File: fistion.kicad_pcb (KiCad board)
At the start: 2 copper layers, 226 x 66.2 mm, 85 parts, among them J1 debug-port, J10 Conn_01x06_Male, J2 USB_C_Receptacle_USB2.0, J3 Conn_01x06_Male, J4 Conn_01x06_Male, J5 Conn_01x06_Male, J6 Conn_01x06_Male, J7 Conn_01x06_Male, J8 Conn_01x06_Male, J9 Conn_01x06_Male, K1 diode-choc, K10 diode-choc, K11 diode-choc, K12 diode-choc, K13 diode-choc, K14 diode-choc, K15 diode-choc, K16 diode-choc, K2 diode-choc, K3 diode-choc, K4 diode-choc, K5 diode-choc, K6 diode-choc, K7 diode-choc, K8 diode-choc, K9 diode-choc, SW1 SW_Push, U1 MT25QL128ABA1ESE, U2 ms88sf3-nrf52840, U3 LSM6DS3, U4 XC6220B331MR, U5 TLV70237_SOT23-5, U6 SRV05-4, U8 PMW3610, U9 MCP1804x-1802xMB

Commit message: no screen
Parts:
- removed JP2: jumper, Jumper:SolderJumper-3_P1.3mm_Open_RoundedPad1.0x1.5mm
- removed JP3: ~, Jumper:SolderJumper-2_P1.3mm_Open_RoundedPad1.0x1.5mm
- removed JP4: SolderJumper_2_Open, Jumper:SolderJumper-2_P1.3mm_Open_RoundedPad1.0x1.5mm
- removed LCD1: adafruit-sharp-memory-display-no-useless, display:adafruit-sharp-memory-display-1.3in-no-mounting-no-useless
- added R7: 1M, Resistor_SMD:R_0603_1608Metric, F.Cu at (120.5, 105.7)
- added REF**: MountingHole_2.2mm_M2, MountingHole:MountingHole_2.2mm_M2, F.Cu at (108.7, 81.7)
- added REF**: MountingHole_2.2mm_M2, MountingHole:MountingHole_2.2mm_M2, F.Cu at (106.2, 115.7)
- added REF**: MountingHole_2.2mm_M2, MountingHole:MountingHole_2.2mm_M2, F.Cu at (136.7, 115.7)
- added REF**: MountingHole_2.2mm_M2, MountingHole:MountingHole_2.2mm_M2, F.Cu at (109.7, 37.7)
- added REF**: nothing, misc:nothing, F.Cu at (82.7, 54.2)
- added REF**: MountingHole_2.2mm_M2, MountingHole:MountingHole_2.2mm_M2, F.Cu at (134.2, 82.2)
- added REF**: MountingHole_2.2mm_M2, MountingHole:MountingHole_2.2mm_M2, F.Cu at (133.2, 37.7)
- added SW2: RotaryEncoder_Switch, switch:EVQWGD001, F.Cu at (121.5, 77.7)
- C4: footprint Capacitor_THT:CP_Radial_D13.0mm_P5.00mm -> Capacitor_THT:CP_Radial_D16.0mm_P7.50mm
- C8: value 47uF -> 4.7uF
- moved D2 142.4 mm to (96.6, 26.5)
- moved J10 142.4 mm to (130.6, 20.3)
- moved J3 142.4 mm to (58.6, 20.3)
- moved J4 142.4 mm to (92.6, 20.3)
- moved J6 142.4 mm to (90.6, 20.3)
- moved K13 142.4 mm to (74.6, 15.9)
- moved K16 142.4 mm to (109.7, 15.9)
- moved SC1 142.4 mm to (109.7, 20.3)
- moved J7 142.4 mm to (162.6, 20.3)
- moved J9 142.4 mm to (128.6, 20.3)
- moved K15 142.4 mm to (146.6, 15.9)
- moved JP1 24.7 mm to (122.0, 96.8), turned to 180 degrees
- moved U4 23.8 mm to (120.7, 100.5), turned to 90 degrees
- moved R21 23.7 mm to (124.2, 111.3)
- moved R22 23.7 mm to (124.2, 112.8)
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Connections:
- J5 pad 6: 3V3_nRF -> +3V3
- JP1 pad 1: 3V3_nRF -> +3V3
- R1 pad 1: 3V3_nRF -> +3V3
- U1 pad 8: 3V3_nRF -> +3V3
- U2 pad 21: DISP_~{CS} -> unconnected-(U2-Pad21)
- U2 pad 22: unconnected-(U2-Pad22) -> MOTION
- U2 pad 23: MOTION -> MOUSE_~{RST}
- U2 pad 24: MOUSE_~{RST} -> MOUSE_~{CS}
- U2 pad 25: MOUSE_~{CS} -> SCLK2
- U2 pad 26: SCLK2 -> SDIO
- U2 pad 27: SDIO -> B
- U2 pad 29: unconnected-(U2-Pad29) -> A
- U2 pad 30: unconnected-(U2-Pad30) -> ENC_PUSH
- U4 pad 3: SOLAR_OUT -> Net-(R7-Pad1)
- U7 pad 11: unconnected-(U7-Pad11) -> Net-(R7-Pad1)
- U9 pad 3: Net-(JP2-Pad2) -> SOLAR_OUT
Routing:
- net +3V3: track 0.00 -> 80.4 mm, vias 0 -> 2
- net 3V3_nRF: track 130.6 -> 78.0 mm, vias 4 -> 1
- net GND: track 11.8 -> 57.0 mm, vias 22 -> 31
- net ENC_PUSH: track 0.00 -> 40.0 mm, vias 0 -> 1
- net A: track 0.00 -> 38.7 mm, vias 0 -> 1
- net B: track 0.00 -> 37.2 mm, vias 0 -> 1
- net C2: track 168.1 -> 148.2 mm
- net +1V8: track 23.8 -> 5.05 mm
- net DISP_~{CS}: track 15.0 -> 0.00 mm, vias 1 -> 0
- net C3: track 139.3 -> 124.4 mm
- net Net-(R7-Pad1): track 0.00 -> 13.8 mm
- net SOLAR_OUT: track 57.8 -> 71.3 mm, vias 0 -> 2
- net BAT: track 85.6 -> 98.8 mm, vias 3 -> 4
- net SDIO: track 45.1 -> 34.3 mm
- net SCLK2: track 45.0 -> 35.3 mm
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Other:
- board size 226 x 66.2 mm -> 104 x 106.5 mm
- board text added: "- screen may go on top/left side"
- board text removed: "- solar & LED goes on top (top thumb?) - screen may go on top/left side"

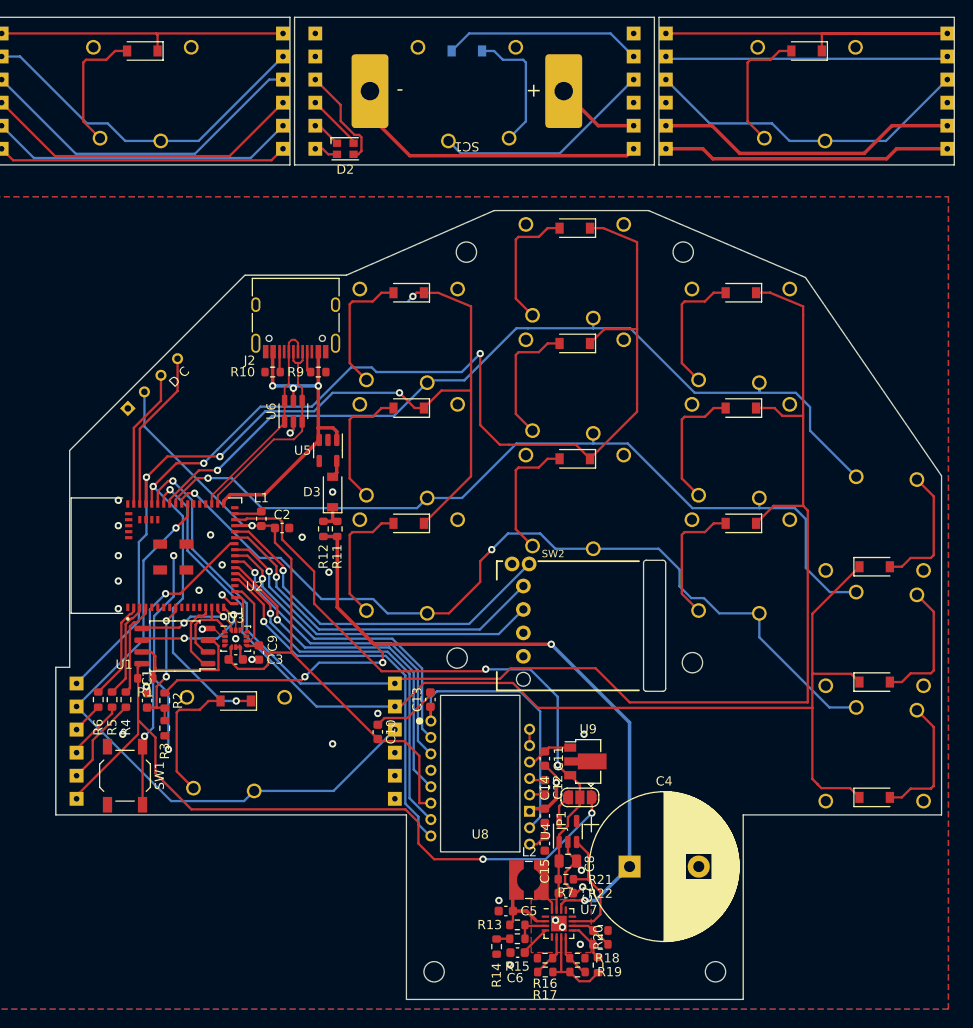
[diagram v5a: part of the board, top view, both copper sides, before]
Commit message: scroll wheel + constant current charger
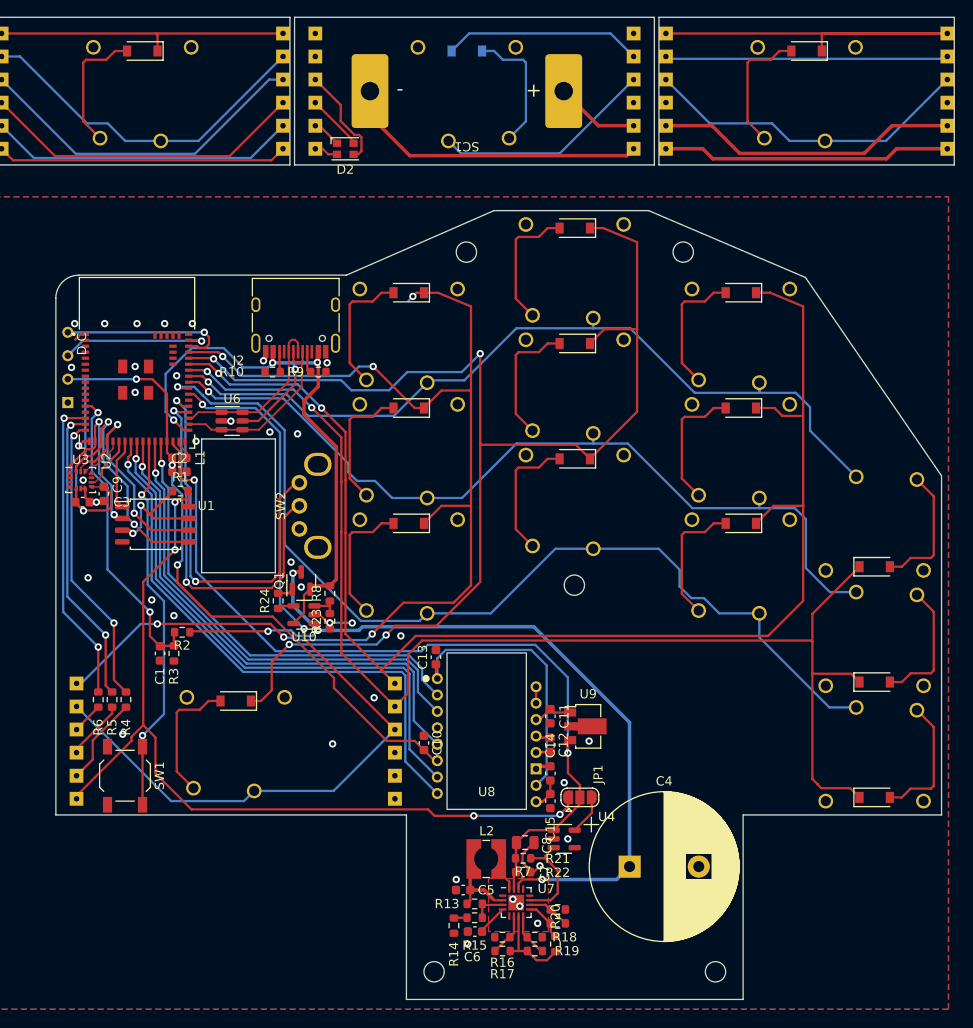
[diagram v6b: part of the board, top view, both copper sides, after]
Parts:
- removed D3: D, Diode_SMD:D_SOD-123
- removed R11, R12: 22, Resistor_SMD:R_0603_1608Metric
- removed the REF** at (82.7, 54.2)
- removed the REF** at (134.2, 82.2)
- removed U5: TLV70237_SOT23-5, Package_TO_SOT_SMD:SOT-23-5
- added Q1: BC807, Package_TO_SOT_SMD:SOT-23, F.Cu at (91.8, 73.3)
- added R23: 8.2k, Resistor_SMD:R_0603_1608Metric, F.Cu at (94.9, 77.7)
- added R24: 2.8k, Resistor_SMD:R_0603_1608Metric, F.Cu at (89.3, 75.5)
- added R8: 2.8k, Resistor_SMD:R_0603_1608Metric, F.Cu at (94.9, 74.7)
- added U10: LM397, Package_TO_SOT_SMD:SOT-23-5, F.Cu at (92.1, 77.0)
- SW2: value RotaryEncoder_Switch -> RotaryEncoder; footprint switch:EVQWGD001 -> switch:EC10E
- moved SW2 30.6 mm to (93.6, 65.2), turned to 90 degrees
- moved C9 24.0 mm to (70.4, 63.9)
- moved U3 24.0 mm to (67.9, 62.4)
- moved C3 23.8 mm to (68.1, 64.8)
- moved U2 21.0 mm to (74.0, 49.7), turned to 0 degrees
- moved R1 20.7 mm to (78.7, 63.6), turned to 180 degrees
- moved REF** 15.0 mm to (121.4, 73.8)
- moved U1 13.4 mm to (76.0, 67.2), turned to 0 degrees
- moved C2 12.7 mm to (78.6, 61.5)
- moved L1 11.1 mm to (78.6, 60.0), turned to 180 degrees
- moved J1 9.36 mm to (66.5, 50.2), turned to 90 degrees
- moved R3 8.16 mm to (78.0, 81.2)
- moved R2 7.64 mm to (78.9, 78.9), turned to 180 degrees
- moved U6 6.73 mm to (84.3, 56.0), turned to 0 degrees
- moved C1 5.29 mm to (76.5, 81.2), turned to -90 degrees
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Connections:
- U2 pad 13: unconnected-(U2-Pad13) -> BAT_MEAS
- U2 pad 14: FLASH_~{CS} -> unconnected-(U2-Pad14)
- U2 pad 15: MISO_DQ1 -> ~{BLUE}
- U2 pad 16: MOSI_DQ0 -> ~{GREEN}
- U2 pad 17: SCLK -> ~{RED}
- U2 pad 19: IMU_~{CS} -> MISO_DQ1
- U2 pad 2: ~{BLUE} -> unconnected-(U2-Pad2)
- U2 pad 20: IMU_INT -> MOSI_DQ0
- U2 pad 21: unconnected-(U2-Pad21) -> SCLK
- U2 pad 22: MOTION -> IMU_~{CS}
- U2 pad 23: MOUSE_~{RST} -> IMU_INT
- U2 pad 24: MOUSE_~{CS} -> FLASH_~{CS}
- U2 pad 25: SCLK2 -> MOTION
- U2 pad 26: SDIO -> MOUSE_~{RST}
- U2 pad 27: B -> MOUSE_~{CS}
- U2 pad 29: A -> SCLK2
- U2 pad 3: ~{GREEN} -> unconnected-(U2-Pad3)
- U2 pad 30: ENC_PUSH -> SDIO
- U2 pad 38: unconnected-(U2-Pad38) -> B
- U2 pad 39: unconnected-(U2-Pad39) -> A
- U2 pad 4: ~{RED} -> unconnected-(U2-Pad4)
- U2 pad 9: BAT_MEAS -> unconnected-(U2-Pad9)
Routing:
- net ENC_PUSH: track 40.0 -> 0.00 mm, vias 1 -> 0
- net GND: track 57.0 -> 18.7 mm, vias 31 -> 38
- net VBUS: track 36.1 -> 71.6 mm, vias 3 -> 4
- net C0: track 102.0 -> 126.4 mm, vias 4 -> 6
- net ~{BLUE}: track 10.9 -> 33.6 mm, vias 0 -> 2
- net ~{GREEN}: track 10.5 -> 32.7 mm, vias 0 -> 2
- net R3: track 68.9 -> 91.0 mm, vias 1 -> 2
- net ~{RED}: track 10.2 -> 31.8 mm, vias 0 -> 2
- net MOTION: track 42.5 -> 62.3 mm
- net SOLAR_OUT: track 71.3 -> 90.7 mm
- net MOUSE_~{RST}: track 41.3 -> 60.1 mm
- net BAT_MEAS: track 15.0 -> 33.2 mm
- net MOUSE_~{CS}: track 38.1 -> 56.2 mm
- net 3V3_nRF: track 78.0 -> 94.7 mm, vias 1 -> 4
- net SCLK2: track 35.3 -> 52.0 mm
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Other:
- outline, holes or cut-outs redrawn

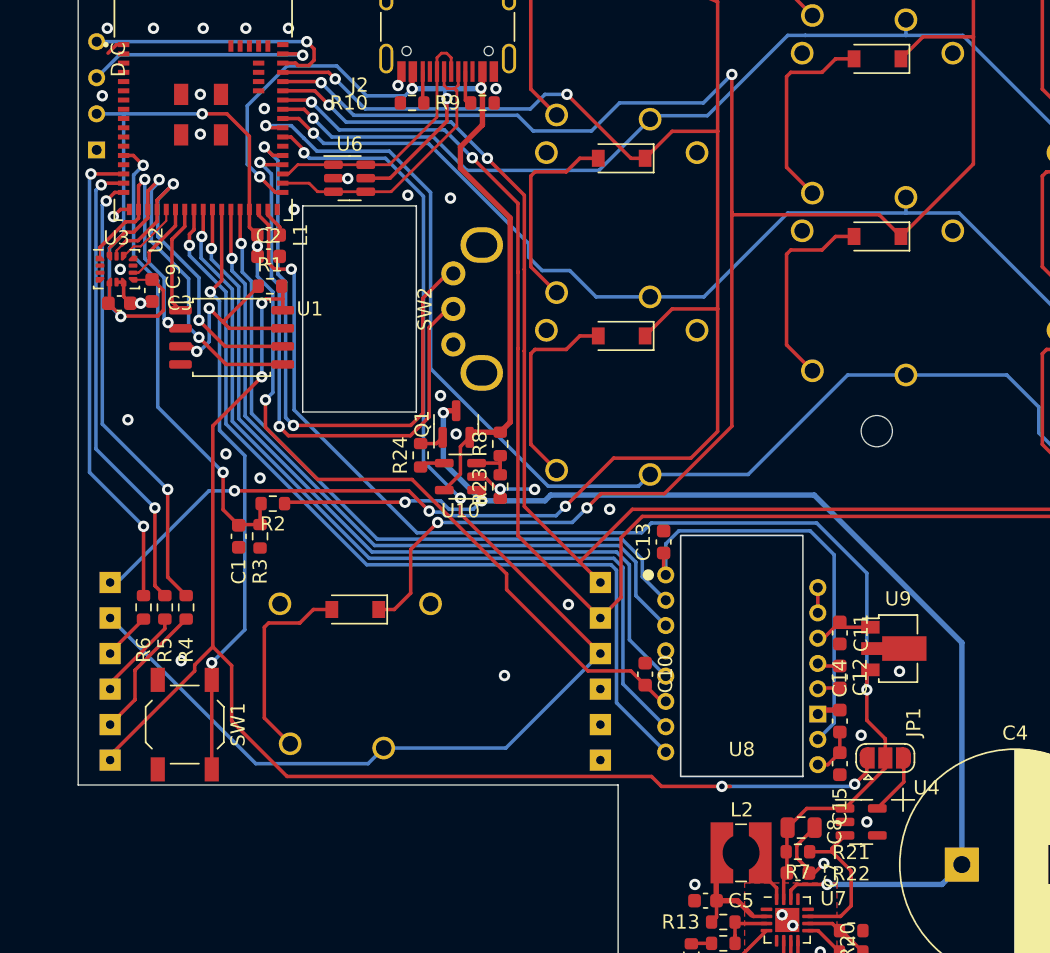
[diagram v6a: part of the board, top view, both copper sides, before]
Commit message: routed with encoder model
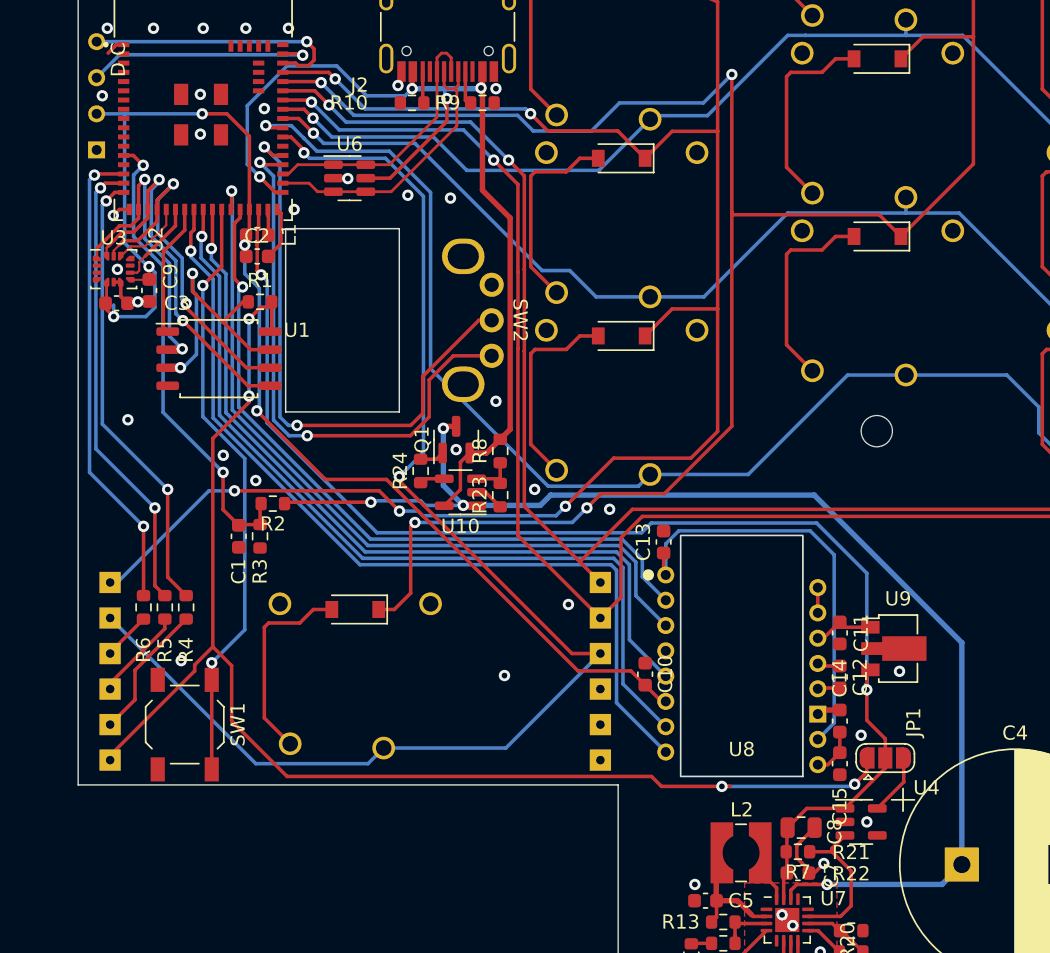
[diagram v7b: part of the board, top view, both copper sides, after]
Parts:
- moved U1 1.75 mm to (75.1, 68.7)
- moved SW2 1.53 mm to (92.3, 66.0), turned to -90 degrees
- moved R1 1.30 mm to (78.0, 64.7)
- moved Q1 1.10 mm to (91.8, 74.4)
- moved R24 1.10 mm to (89.3, 76.6)
- moved U10 1.10 mm to (92.1, 78.1)
- moved C2 0.80 mm to (77.8, 61.5)
- moved L1 0.80 mm to (77.8, 60.0)
- moved R23 0.60 mm to (94.9, 78.3)
- moved R8 0.50 mm to (94.9, 75.2)
- moved C9 0.20 mm to (70.2, 63.9)
- moved U3 0.20 mm to (67.7, 62.4)
- moved C3 0.20 mm to (67.9, 64.8)
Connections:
- U2 pad 38: B -> A
- U2 pad 39: A -> B
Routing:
- net Net-(R1-Pad2): track 14.1 -> 19.0 mm
- net MISO_DQ1: track 18.6 -> 21.5 mm
- net SCLK2: track 52.0 -> 54.9 mm
- net R3: track 91.0 -> 93.6 mm
- net 3V3_nRF: track 94.7 -> 92.5 mm, vias 4 -> 5
- net A: track 42.0 -> 39.9 mm
- net FLASH_~{CS}: track 7.72 -> 9.34 mm
- net BAT: track 90.8 -> 89.3 mm
- net C1: track 140.9 -> 141.8 mm
- net C0: track 126.4 -> 125.6 mm
- net SDIO: track 50.0 -> 50.8 mm
- net C2: track 147.0 -> 147.8 mm
- net SOLAR_OUT: track 90.7 -> 91.5 mm
- net C3: track 138.4 -> 139.2 mm
- net +3V3: track 93.9 -> 93.2 mm
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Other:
- outline, holes or cut-outs redrawn
